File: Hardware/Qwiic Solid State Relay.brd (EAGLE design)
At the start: 185.4 x 86.4 mm, 49 parts, among them J2 Qwiic Right Angle, J3 Qwiic Right Angle, J9 AVR_SPI_PROG_3X2TESTPOINTS, K1 Solid State Relay - 40A, K2 Solid State Relay - 40A, K3 Solid State Relay - 40A, K4 Solid State Relay - 40A, Q1 600mA/40V, Q2 600mA/40V, Q3 600mA/40V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

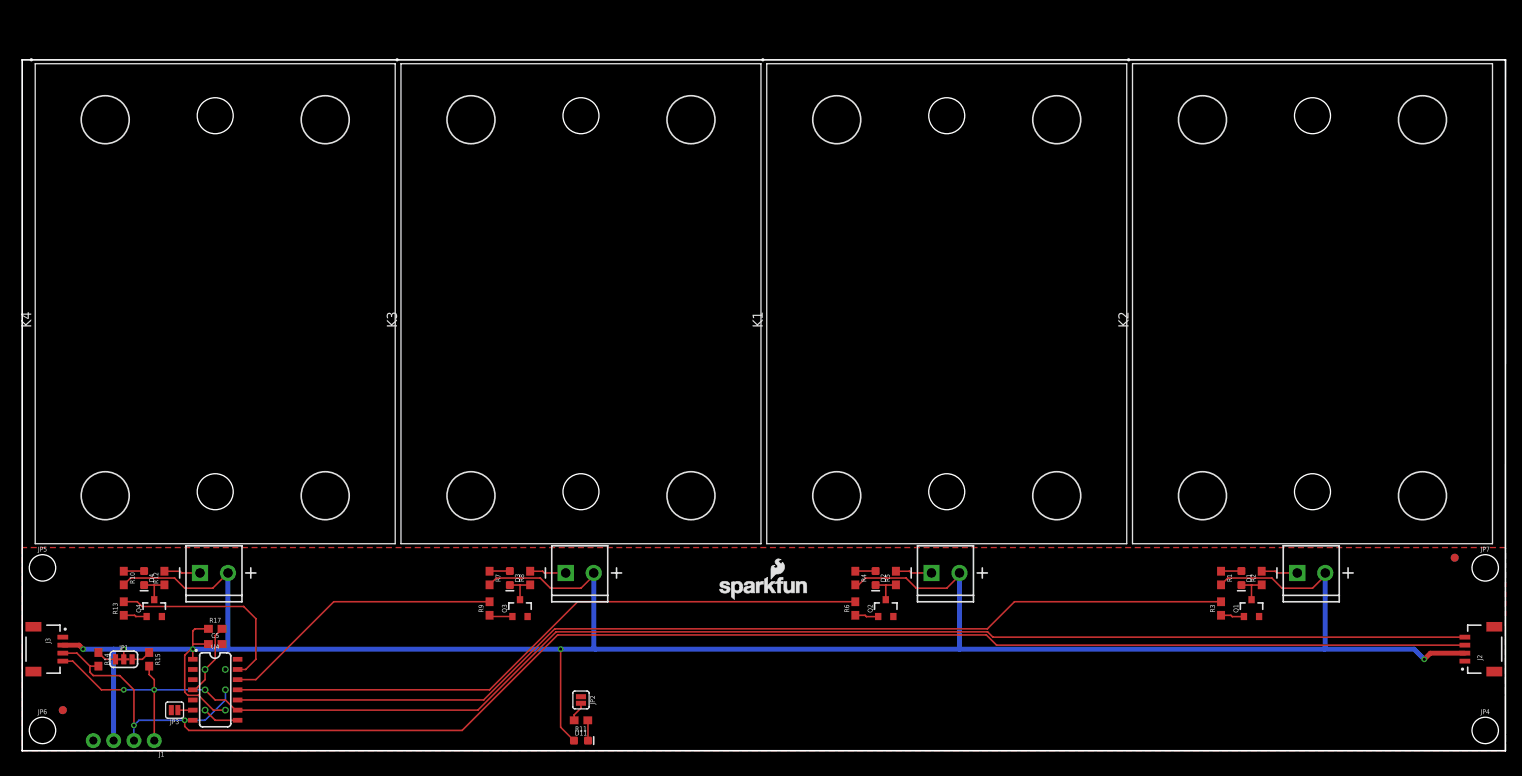
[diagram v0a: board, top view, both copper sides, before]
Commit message: adding silk
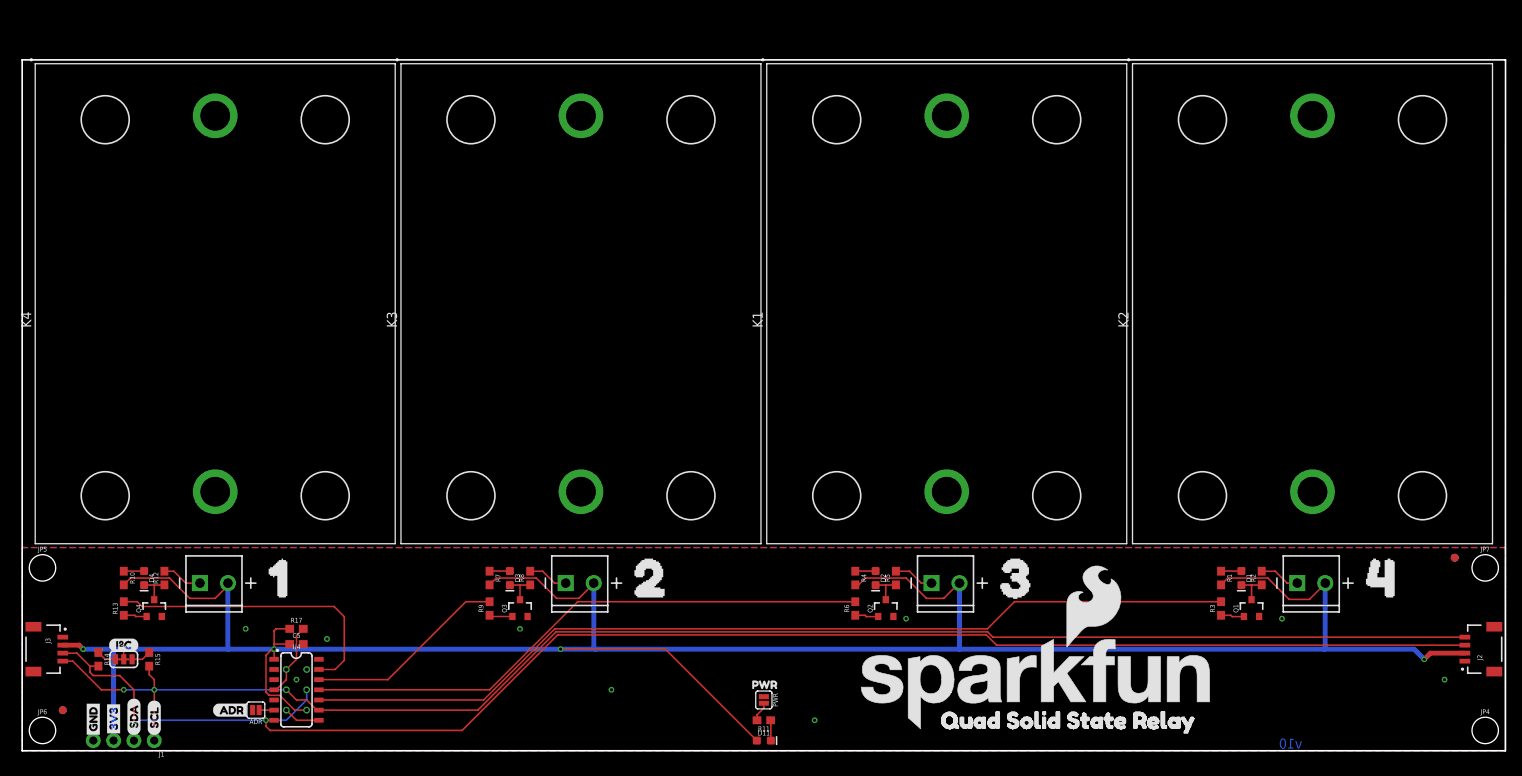
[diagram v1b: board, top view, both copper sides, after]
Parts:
- removed JP2, JP3: JUMPER-SMT_2_NO_SILK, SparkFun-Jumpers:SMT-JUMPER_2_NO_SILK
- added ADR, PWR: JUMPER-SMT_2_NO_SILK, SparkFun-Jumpers:SMT-JUMPER_2_NO_SILK
- added U$1: (no value), SparkFun-Aesthetics:SFE_LOGO_NAME_FLAME_.4
- added U$10, U$6: (no value), buzzard_labels (11):22
- added U$11, U$7: (no value), buzzard_labels (11):33
- added U$12, U$8: (no value), buzzard_labels (11):44
- added U$13, U$14: (no value), SparkFun-Buzzard:GND_P
- added U$15: (no value), SparkFun-Buzzard:I2C
- added U$16, U$17: (no value), SparkFun-Buzzard:3V3_P
- added U$18, U$19: (no value), SparkFun-Buzzard:SCL_IO
- added U$2: (no value), buzzard_labels (11):QUAD_SOLID_STATE_RELAY0
- added U$20, U$21: (no value), SparkFun-Buzzard:SDA_IO
- added U$22: (no value), SparkFun-Buzzard:PWR_TO
- added U$23: (no value), buzzard_labels (13):ADR3
- added U$3, U$4: (no value), buzzard_labels (10):QUAD_SOLID_STATE_RELAY0
- added U$5, U$9: (no value), buzzard_labels (11):11
- LOGO1: value SFE_LOGO_NAME_FLAME.1_INCH -> SFE_LOGO_NAME1_INCH; device SparkFun-Aesthetics:SFE_LOGO_NAME_FLAME_.1 -> SparkFun-Aesthetics:SFE_LOGO_NAME_1
- R12, R2, R5, R8: value 33 -> 47
- moved LOGO1 59.2 mm to (147.3, 43.2), flipped to the bottom
- moved D11 22.9 mm to (92.7, 1.27)
- moved R11 22.9 mm to (92.7, 3.81)
- moved C5 10.2 mm to (34.3, 13.3)
- moved J9 10.2 mm to (34.3, 7.62)
- moved R17 10.2 mm to (34.3, 15.2)
- moved U4 10.2 mm to (34.3, 7.62)
- renumbered JP1 to I2C
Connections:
- net ADDR_JUMP: now also ADR.1; no longer JP3.1
- net GND: now also ADR.2, PWR.1; no longer JP2.1, JP3.2
- net N$14: now also PWR.2; no longer JP2.2
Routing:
- net 3.3V: track 318.2 -> 332.2 mm
- net RELAY_CTRL4: track 25.3 -> 37.4 mm
- net RELAY_CTRL3: track 35.5 -> 25.4 mm
- net RELAY_CTRL2: track 81.8 -> 71.6 mm
- net RELAY_CTRL1: track 128.0 -> 117.9 mm
- net N$6: track 4.53 -> 5.06 mm
- net N$3: track 4.53 -> 5.06 mm
- net N$11: track 4.53 -> 5.06 mm
- net N$10: track 4.53 -> 5.06 mm
- added copper zone on layer 16, net GND
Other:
- board text added: "v10"

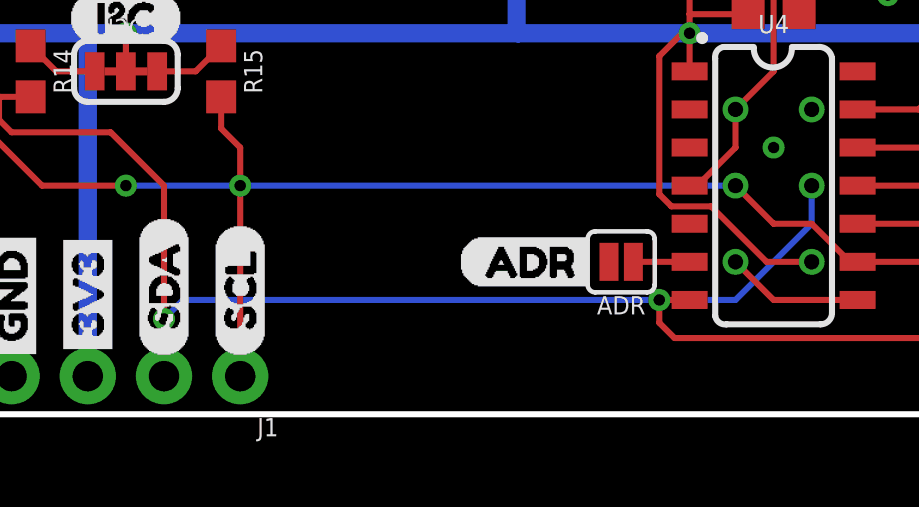
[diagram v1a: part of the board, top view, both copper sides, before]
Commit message: fixing overlap error, wire stub
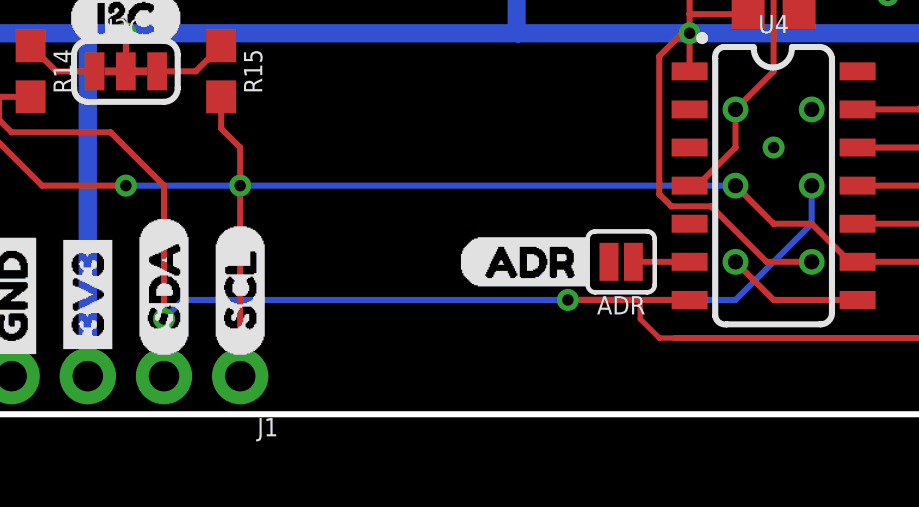
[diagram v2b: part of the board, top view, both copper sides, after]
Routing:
- net SDA/MOSI: track 200.5 -> 206.0 mm
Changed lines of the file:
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@@
 <contactref element="J1" pad="2"/>
 <contactref element="U4" pad="7"/>
-<wire x1="31.49" y1="3.81" x2="31.871" y2="3.81" width="0.2032" layer="1"/>
-<wire x1="31.49" y1="3.81" x2="30.48" y2="3.81" width="0.2032" layer="1"/>
-<via x="30.48" y="3.81" extent="1-16" drill="0.381"/>
-<wire x1="30.48" y1="3.81" x2="14.605" y2="3.81" width="0.2032" layer="16"/>
+<wire x1="31.49" y1="3.81" x2="29.845" y2="3.81" width="0.2032" layer="1"/>
+<via x="27.432" y="3.81" extent="1-16" drill="0.381"/>
+<wire x1="29.845" y1="3.81" x2="27.432" y2="3.81" width="0.2032" layer="1"/>
+<wire x1="27.432" y1="3.81" x2="14.605" y2="3.81" width="0.2032" layer="16"/>
 <wire x1="13.97" y1="3.175" x2="13.97" y2="1.27" width="0.2032" layer="16"/>
 <wire x1="14.605" y1="3.81" x2="13.97" y2="3.175" width="0.2032" layer="16"/>
 <wire x1="35.56" y1="7.62" x2="35.56" y2="6.35" width="0.2032" layer="16"/>
 <wire x1="35.56" y1="6.35" x2="33.02" y2="3.81" width="0.2032" layer="16"/>
-<wire x1="33.02" y1="3.81" x2="30.48" y2="3.81" width="0.2032" layer="16"/>
+<wire x1="33.02" y1="3.81" x2="27.432" y2="3.81" width="0.2032" layer="16"/>
 <contactref element="R14" pad="2"/>
 <wire x1="12.192" y1="9.398" x2="13.97" y2="7.62" width="0.2032" layer="1"/>
@@
 <wire x1="180.34" y1="13.2" x2="121.801" y2="13.2" width="0.2032" layer="1"/>
 <wire x1="121.801" y1="13.2" x2="120.523" y2="14.478" width="0.2032" layer="1"/>
-<wire x1="30.988" y1="2.54" x2="30.48" y2="3.048" width="0.2032" layer="1"/>
-<wire x1="30.48" y1="3.048" x2="30.48" y2="3.81" width="0.2032" layer="1"/>
+<wire x1="29.718" y1="3.81" x2="27.432" y2="3.81" width="0.2032" layer="1"/>
 <wire x1="120.523" y1="14.478" x2="66.929" y2="14.478" width="0.2032" layer="1"/>
 <wire x1="66.929" y1="14.478" x2="54.991" y2="2.54" width="0.2032" layer="1"/>
@@
 <wire x1="8.89" y1="9.398" x2="8.47" y2="9.818" width="0.2032" layer="1"/>
 <wire x1="8.47" y1="9.818" x2="8.47" y2="10.58" width="0.2032" layer="1"/>
+<wire x1="30.988" y1="2.54" x2="30.48" y2="2.54" width="0.1778" layer="1"/>
+<wire x1="30.48" y1="2.54" x2="29.845" y2="3.175" width="0.1778" layer="1"/>
+<wire x1="29.845" y1="3.175" x2="29.845" y2="3.81" width="0.1778" layer="1"/>
 </signal>
 <signal name="SCL/SCK">
@@
 <mfgpreviewcolor name="substratecolor" color="0xFF786E46"/>
 </mfgpreviewcolors>
+<errors>
+</errors>
 </board>
 </drawing>

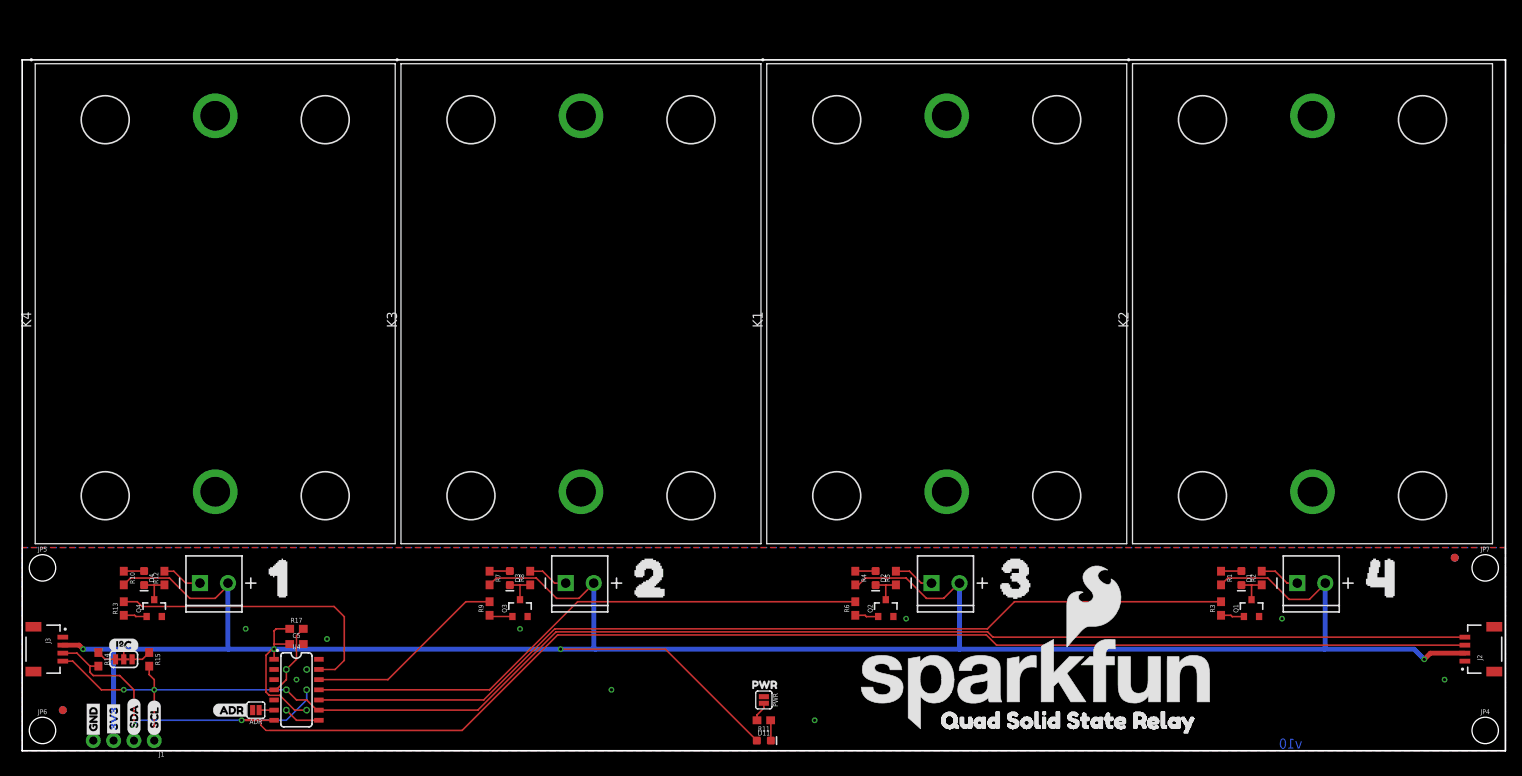
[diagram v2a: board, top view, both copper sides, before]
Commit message: updating for reds after design review, checklist
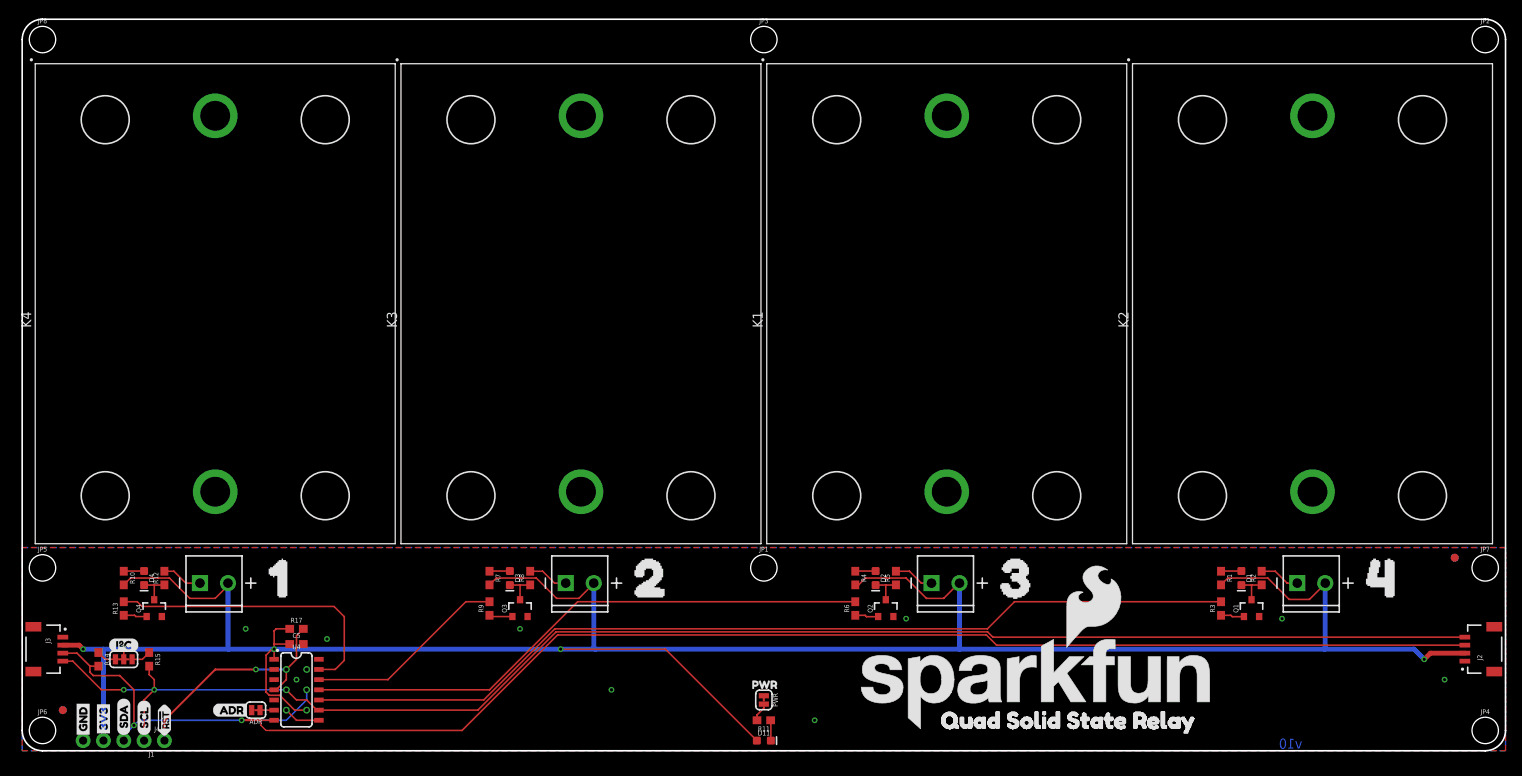
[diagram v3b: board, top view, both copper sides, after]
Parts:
- added J4: (no value), SparkFun-Connectors:1X01_NO_SILK
- added JP1, JP2, JP3, JP8: STAND-OFF, SparkFun-Hardware:STAND-OFF
- added U$24, U$25: (no value), SparkFun-Buzzard:!RST_I
- ADR, PWR: value JUMPER-SMT_2_NO_SILK -> JUMPER-SMT_2_NC_TRACE_SILK; device SparkFun-Jumpers:SMT-JUMPER_2_NO_SILK -> SparkFun-Jumpers:SMT-JUMPER_2_NC_TRACE_SILK
- moved J1 1.27 mm to (15.2, 1.27)
- moved U$18 1.27 mm to (15.2, 1.91)
- moved U$19 1.27 mm to (15.2, 1.91)
- moved U$20 1.27 mm to (12.7, 1.91)
- moved U$21 1.27 mm to (12.7, 1.91)
- moved U$13 1.27 mm to (7.62, 1.52)
- moved U$14 1.27 mm to (7.62, 1.52)
- moved U$16 1.27 mm to (10.2, 1.65)
- moved U$17 1.27 mm to (10.2, 1.65)
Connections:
- net !RESET: now also J4.1
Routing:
- net !RESET: track 9.28 -> 29.7 mm, vias 0 -> 1
- net SCL/SCK: track 191.7 -> 192.2 mm
- net SDA/MOSI: track 206.0 -> 206.6 mm
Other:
- board size 185.4 x 86.4 mm -> 185.4 x 91.4 mm
- board text added: "Andy England"

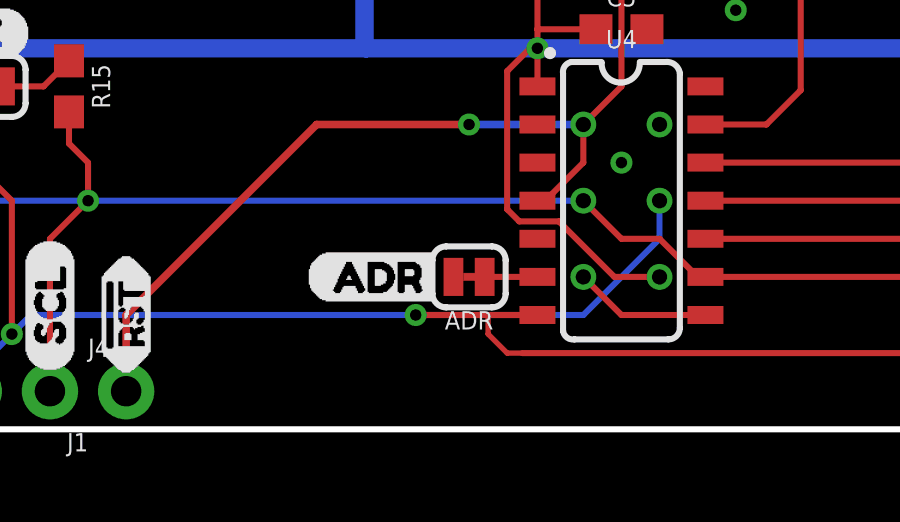
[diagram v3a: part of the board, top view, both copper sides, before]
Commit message: forgot to save brd file for previous commit
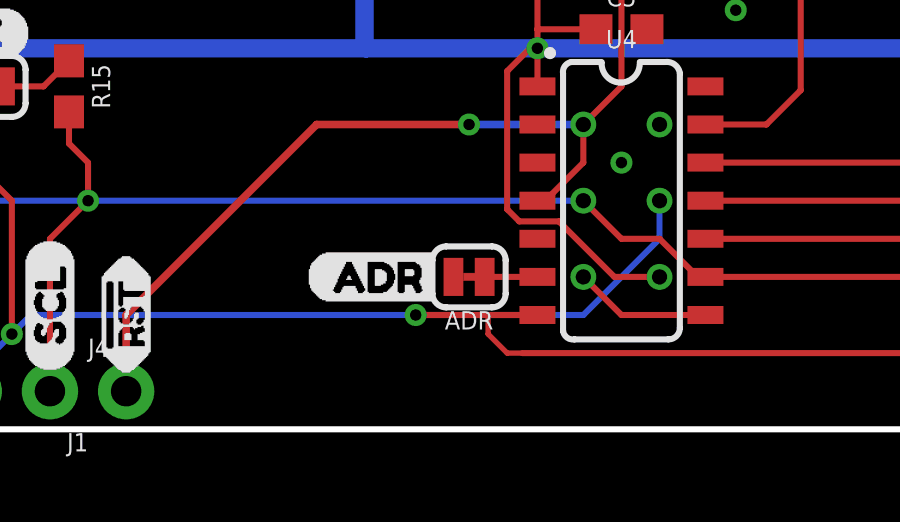
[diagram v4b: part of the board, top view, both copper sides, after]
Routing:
- net SDA/MOSI: track 206.6 -> 204.3 mm
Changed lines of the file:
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@@
 <layer number="45" name="Holes" color="7" fill="1" visible="yes" active="yes"/>
 <layer number="46" name="Milling" color="3" fill="1" visible="no" active="yes"/>
-<layer number="47" name="Measures" color="7" fill="1" visible="no" active="yes"/>
+<layer number="47" name="Measures" color="7" fill="1" visible="yes" active="yes"/>
 <layer number="48" name="Document" color="7" fill="1" visible="no" active="yes"/>
 <layer number="49" name="Reference" color="7" fill="1" visible="no" active="yes"/>
@@
 <wire x1="182.88" y1="91.44" x2="185.42" y2="88.9" width="0.2032" layer="20" curve="-90"/>
 <wire x1="185.42" y1="2.54" x2="182.88" y2="0" width="0.2032" layer="20" curve="-90"/>
+<dimension x1="0" y1="0" x2="185.42" y2="0" x3="92.71" y3="-5.08" textsize="1.778" layer="47" unit="inch"/>
+<dimension x1="2.54" y1="2.54" x2="0" y2="2.54" x3="1.27" y3="-2.54" textsize="1.778" layer="47" unit="inch"/>
+<dimension x1="2.54" y1="22.86" x2="2.54" y2="0" x3="-2.54" y3="11.43" textsize="1.778" layer="47" unit="inch"/>
+<dimension x1="0" y1="0" x2="0" y2="91.44" x3="-7.62" y3="45.72" textsize="1.778" layer="47" unit="inch"/>
+<dimension x1="2.54" y1="88.9" x2="2.54" y2="91.44" x3="-1.27" y3="90.17" textsize="1.778" layer="47" unit="inch"/>
+<dimension x1="0" y1="88.9" x2="92.71" y2="88.9" x3="46.355" y3="96.52" textsize="1.778" layer="47" unit="inch"/>
 </plain>
 <attributes>
@@
 <wire x1="180.34" y1="13.2" x2="121.801" y2="13.2" width="0.2032" layer="1"/>
 <wire x1="121.801" y1="13.2" x2="120.523" y2="14.478" width="0.2032" layer="1"/>
-<wire x1="29.718" y1="3.81" x2="27.432" y2="3.81" width="0.2032" layer="1"/>
 <wire x1="120.523" y1="14.478" x2="66.929" y2="14.478" width="0.2032" layer="1"/>
 <wire x1="66.929" y1="14.478" x2="54.991" y2="2.54" width="0.2032" layer="1"/>
